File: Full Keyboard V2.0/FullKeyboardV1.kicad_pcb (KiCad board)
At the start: 2 copper layers, 305.6 x 104.9 mm, 624 parts, among them J1 Conn_01x26, J2 USB_C_Receptacle_USB2.0, P7 AMS1117, SW1 Esc, SW10 2, SW11 W, SW12 S, SW13 Z, SW15 3, SW16 E, SW17 D, SW18 X, SW19 4, SW2 Tab, SW20 R, SW21 F, SW22 C, SW23 5, SW24 T, SW25 G, SW26 V, SW27 6, SW28 Y, SW29 H, SW3 Caps, SW30 B, SW32 7, SW33 U, SW34 J, SW35 N, SW36 8, SW37 I, SW38 K, SW39 M, SW4 LShift, SW40 9, SW41 O, SW42 L, SW43 <, SW44 0, SW45 P, SW46 ;, SW47 >, SW49 Minus, SW5 End/Home, SW50 [, SW51 ", SW52 /, SW54 =, SW55 ], SW56 Up, SW57 RShift, SW59 BKSPC, SW6 1, SW60 \, SW61 Enter, SW63 Til, SW64 Del, SW65 Pg Up, SW66 Pg Dw, SW7 Q, SW8 A, T1 Vin, T3 Vout, U1 AT24C02, U3 CD74HC4067SM, U5 Cherry_bottom_row

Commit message: Added USB HUB
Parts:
- removed the REF**413 at (190.7, 60.1)
- removed the REF**413 at (180.7, 60.3)
- removed the REF**413 at (22.9, 59.1)
- removed the REF**413 at (41.6, 59.3)
- removed the REF**423 at (191.7, 60.1)
- removed the REF**423 at (42.6, 59.3)
- removed the REF**423 at (181.7, 60.3)
- removed the REF**423 at (23.9, 59.1)
- removed the REF**431 at (61.0, 58.9)
- removed the REF**431 at (80.7, 59.0)
- removed the REF**431 at (99.3, 58.9)
- removed the REF**431 at (118.3, 59.1)
- removed the REF**431 at (137.8, 59.0)
- removed the REF**431 at (157.2, 59.3)
- removed the REF**431 at (186.4, 56.0)
- removed the REF**432 at (129.7, 66.3)
- removed the REF**432 at (62.0, 58.9)
- removed the REF**432 at (81.7, 59.0)
- removed the REF**432 at (100.3, 58.9)
- removed the REF**432 at (119.3, 59.1)
- removed the REF**432 at (138.8, 59.0)
- removed the REF**432 at (158.2, 59.3)
- removed the REF**432 at (187.4, 56.0)
- removed the REF**433 at (159.2, 59.3)
- removed the REF**433 at (188.4, 56.0)
- removed the REF**433 at (129.7, 65.3)
- removed the REF**433 at (24.9, 59.1)
- removed the REF**433 at (43.6, 59.3)
- removed the REF**433 at (192.7, 60.1)
- removed the REF**433 at (182.7, 60.3)
- removed the REF**433 at (63.0, 58.9)
- removed the REF**433 at (82.7, 59.0)
- removed the REF**433 at (101.3, 58.9)
- removed the REF**433 at (120.3, 59.1)
- removed the REF**433 at (139.8, 59.0)
- added C3: 0.1uF, Capacitor_SMD:C_0603_1608Metric, B.Cu at (176.8, 55.6)
- added C74: 10uF, Capacitor_SMD:C_0603_1608Metric, B.Cu at (175.1, 55.6)
- added C75: 10uF, Capacitor_SMD:C_0603_1608Metric, B.Cu at (142.0, 52.0)
- added C76: 0.1uF, Capacitor_SMD:C_0603_1608Metric, B.Cu at (139.2, 52.0)
- added C77: 0.1uF, Capacitor_SMD:C_0603_1608Metric, B.Cu at (144.8, 52.0)
- added C78: 10uF, Capacitor_SMD:C_0603_1608Metric, B.Cu at (136.4, 52.0)
- added D69: Green, LED_SMD:LED_0603_1608Metric, F.Cu at (95.5, 53.0)
- added D73: Green, LED_SMD:LED_0603_1608Metric, F.Cu at (93.8, 53.0)
- added D74: Green, LED_SMD:LED_0603_1608Metric, F.Cu at (99.1, 53.0)
- added D75: Green, LED_SMD:LED_0603_1608Metric, F.Cu at (97.3, 53.0)
- added D76: Red, LED_SMD:LED_0603_1608Metric, F.Cu at (92.0, 53.0)
- added J3: USB_A, Connector_USB:USB_A_Stewart_SS-52100-001_Horizontal, B.Cu at (19.6, 55.1)
- added J4: USB_A, Connector_USB:USB_A_Stewart_SS-52100-001_Horizontal, B.Cu at (37.9, 55.1)
- added J5: USB_A, Connector_USB:USB_A_Stewart_SS-52100-001_Horizontal, B.Cu at (56.1, 55.1)
- added JP3: SolderJumper_2_Open, Jumper:SolderJumper-2_P1.3mm_Open_RoundedPad1.0x1.5mm, B.Cu at (187.8, 54.8)
- added JP4: SolderJumper_2_Open, Jumper:SolderJumper-2_P1.3mm_Open_RoundedPad1.0x1.5mm, B.Cu at (187.8, 51.0)
- added JP5: SolderJumper_2_Bridged, Jumper:SolderJumper-2_P1.3mm_Bridged_RoundedPad1.0x1.5mm, B.Cu at (180.6, 54.8)
- added JP6: SolderJumper_2_Bridged, Jumper:SolderJumper-2_P1.3mm_Bridged_RoundedPad1.0x1.5mm, B.Cu at (184.2, 51.0)
- added JP7: SolderJumper_2_Bridged, Jumper:SolderJumper-2_P1.3mm_Bridged_RoundedPad1.0x1.5mm, B.Cu at (180.6, 51.0)
- added JP8: SolderJumper_2_Bridged, Jumper:SolderJumper-2_P1.3mm_Bridged_RoundedPad1.0x1.5mm, B.Cu at (184.2, 54.8)
- added R10: 330, Resistor_SMD:R_0603_1608Metric, F.Cu at (106.2, 51.8)
- added R13: 330, Resistor_SMD:R_0603_1608Metric, F.Cu at (106.1, 54.8)
- added R14: 330, Resistor_SMD:R_0603_1608Metric, F.Cu at (89.1, 53.6)
- added R5: 100K, Resistor_SMD:R_0603_1608Metric, B.Cu at (176.0, 53.0)
- added R8: 47K, Resistor_SMD:R_0603_1608Metric, B.Cu at (175.8, 51.4)
- added R9: 2K7, Resistor_SMD:R_0603_1608Metric, B.Cu at (175.5, 49.7)
- added REF**431: Stitching-Via-0.6mm, keyboard:Stitching-Via-0.6mm, F.Cu at (239.7, 56.7)
- added REF**431: Stitching-Via-0.6mm, keyboard:Stitching-Via-0.6mm, F.Cu at (241.9, 56.7)
- added REF**431: Stitching-Via-0.6mm, keyboard:Stitching-Via-0.6mm, F.Cu at (248.0, 49.3)
- added REF**431: Stitching-Via-0.6mm, keyboard:Stitching-Via-0.6mm, F.Cu at (223.3, 71.7)
- added REF**432: Stitching-Via-0.6mm, keyboard:Stitching-Via-0.6mm, F.Cu at (223.3, 70.7)
- added REF**432: Stitching-Via-0.6mm, keyboard:Stitching-Via-0.6mm, F.Cu at (192.9, 49.2)
- added REF**432: Stitching-Via-0.6mm, keyboard:Stitching-Via-0.6mm, F.Cu at (192.2, 53.8)
- added REF**432: Stitching-Via-0.6mm, keyboard:Stitching-Via-0.6mm, F.Cu at (192.7, 60.7)
- added REF**433: Stitching-Via-0.6mm, keyboard:Stitching-Via-0.6mm, F.Cu at (223.3, 69.7)
- added REF**433: Stitching-Via-0.6mm, keyboard:Stitching-Via-0.6mm, F.Cu at (193.7, 60.7)
- added U2: FE1.1s, Package_SO:SSOP-28_3.9x9.9mm_P0.635mm, B.Cu at (168.3, 52.6)
- added Y1: 12MHz, Crystal:Crystal_SMD_HC49-SD, B.Cu at (153.6, 51.4)
- moved C2 2.46 mm to (196.3, 59.0)
- moved D40 1.93 mm to (167.0, 64.6), turned to 90 degrees
- moved D44 1.82 mm to (186.0, 64.5), turned to 90 degrees
- moved D36 1.62 mm to (148.1, 64.3), turned to 90 degrees
- moved D32 1.61 mm to (128.9, 64.2), turned to 90 degrees
- moved D10 1.05 mm to (34.2, 63.6), turned to 90 degrees
- moved D27 1.03 mm to (110.0, 63.7), turned to 90 degrees
- moved D15 1.01 mm to (53.1, 63.6), turned to 90 degrees
- moved D6 0.97 mm to (15.2, 63.6), turned to 90 degrees
- moved D23 0.97 mm to (91.0, 63.6), turned to 90 degrees
- moved D19 0.82 mm to (72.0, 63.5), turned to 90 degrees
- moved D1 0.27 mm to (-3.15, 63.0), turned to 90 degrees
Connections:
- J2 pad A6: /MicroSheet/USB+D+ -> /PowerSheet/USB_D+
- J2 pad A7: /MicroSheet/USB_D- -> /PowerSheet/USB_D-
- J2 pad B6: /MicroSheet/USB+D+ -> /PowerSheet/USB_D+
- J2 pad B7: /MicroSheet/USB_D- -> /PowerSheet/USB_D-
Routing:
- net +5V: track 47.9 -> 279.3 mm, vias 1 -> 4
- net Net-(J3-Pad2): track 0.00 -> 155.6 mm, vias 0 -> 2
- net Net-(J3-Pad3): track 0.00 -> 152.9 mm, vias 0 -> 2
- net Net-(J4-Pad2): track 0.00 -> 133.9 mm, vias 0 -> 2
- net Net-(J4-Pad3): track 0.00 -> 132.3 mm, vias 0 -> 2
- net Net-(J5-Pad2): track 0.00 -> 113.9 mm, vias 0 -> 1
- net Net-(J5-Pad3): track 0.00 -> 112.3 mm, vias 0 -> 1
- net /PowerSheet/USB_D+: track 0.00 -> 83.7 mm, vias 0 -> 4
- net Net-(D69-Pad1): track 0.00 -> 80.8 mm, vias 0 -> 1
- net /PowerSheet/USB_D-: track 0.00 -> 76.7 mm, vias 0 -> 4
- net Net-(R13-Pad2): track 0.00 -> 63.5 mm, vias 0 -> 1
- net Net-(R10-Pad2): track 0.00 -> 63.2 mm, vias 0 -> 1
- net Net-(C75-Pad2): track 0.00 -> 39.3 mm, vias 0 -> 4
- net +3V3: track 2497.4 -> 2528.2 mm, vias 74 -> 80
- net GND: track 19.3 -> 39.9 mm, vias 1 -> 2
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
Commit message: Added multi-function left and right shift
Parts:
- removed the REF**41 at (274.6, 130.3)
- removed the REF**41 at (248.4, 130.3)
- removed the REF**411 at (26.4, 122.0)
- removed the REF**411 at (254.2, 123.7)
- removed the REF**412 at (26.4, 123.0)
- removed the REF**412 at (254.2, 124.7)
- removed the REF**413 at (26.4, 124.0)
- removed the REF**413 at (5.54, 136.3)
- removed the REF**421 at (27.4, 122.0)
- removed the REF**421 at (255.2, 123.7)
- removed the REF**422 at (27.4, 123.0)
- removed the REF**422 at (255.2, 124.7)
- removed the REF**422 at (6.54, 135.3)
- removed the REF**423 at (27.4, 124.0)
- removed the REF**423 at (255.2, 125.7)
- removed the REF**431 at (28.4, 122.0)
- removed the REF**431 at (7.54, 134.3)
- removed the REF**432 at (28.4, 123.0)
- removed the REF**432 at (256.2, 124.7)
- removed the REF**433 at (28.4, 124.0)
- removed the REF**433 at (256.2, 125.7)
- removed SW56: Up, keyboard:RGB_CHERRY_PCB_100H
- removed SW57: RShift, keyboard:RGB_CHERRY_PCB_175H
- added C79: C_Small, Capacitor_SMD:C_0603_1608Metric, B.Cu at (21.1, 127.7)
- added D77: D_Small, Diode_SMD:D_SOD-123, B.Cu at (22.2, 116.0)
- added REF**41: Stitching-Via-0.6mm, keyboard:Stitching-Via-0.6mm, F.Cu at (32.1, 130.2)
- added SW9: double_key, keyboard:RGB_CHERRY_SHIFT_RIGHT_2.0, F.Cu at (252.4, 123.9)
- SW4: value LShift -> double_key; footprint keyboard:RGB_CHERRY_PCB_200H -> keyboard:RGB_CHERRY_SHIFT_ROW_LEFT
- moved C6 9.63 mm to (0.01, 129.0), turned to 90 degrees
- moved REF**41 8.97 mm to (11.2, 130.3)
- moved D4 5.96 mm to (9.66, 116.0)
- moved C61 4.11 mm to (241.3, 126.3)
- moved D57 3.07 mm to (237.0, 117.2)
- moved D56 1.22 mm to (261.0, 119.1)
- moved D9 1.13 mm to (21.1, 136.6)
- moved SW4 0.05 mm to (15.8, 123.9)
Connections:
- SW4 pad 3: +3V3 -> /ROW3
- SW4 pad 5: GND -> +3V3
- SW4 pad 6: Net-(SW13-Pad4) -> Net-(SW4-Pad6)
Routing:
- net Net-(SW56-Pad4): track 22.1 -> 0.00 mm, vias 2 -> 0
- net +3V3: track 2528.2 -> 2548.4 mm, vias 80 -> 81
- net Net-(SW13-Pad4): track 26.8 -> 10.5 mm
- net Net-(SW9-Pad10): track 0.00 -> 13.6 mm, vias 0 -> 2
- net Net-(SW4-Pad10): track 0.00 -> 13.0 mm, vias 0 -> 2
- net Net-(D4-Pad1): track 3.26 -> 15.1 mm
- net Net-(D57-Pad1): track 2.61 -> 13.9 mm
- net /ROW3: track 360.3 -> 369.9 mm
- net /COL0: track 291.6 -> 298.5 mm
- net Net-(D77-Pad1): track 0.00 -> 4.31 mm
- net Net-(SW66-Pad4): track 14.8 -> 10.8 mm
- net /COL1: track 276.1 -> 279.0 mm
- net /COL12: track 109.2 -> 106.7 mm
- net /COL13: track 136.0 -> 137.6 mm
- net Net-(D9-Pad1): track 6.98 -> 8.55 mm
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
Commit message: Added solder jumpers to allow for daisy chaining RGB rows
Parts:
- removed LCD2: SPI_spare, Connector_PinHeader_2.54mm:PinHeader_1x04_P2.54mm_Vertical_SMD_Pin1Left
- removed the REF**411 at (282.3, 53.2)
- removed the REF**421 at (282.3, 52.2)
- removed the REF**421 at (203.0, 97.4)
- removed the REF**431 at (239.7, 56.7)
- removed the REF**431 at (248.5, 53.3)
- removed the REF**431 at (203.0, 98.4)
- removed the REF**431 at (241.9, 56.7)
- removed the REF**431 at (248.0, 49.3)
- removed the REF**431 at (282.3, 51.2)
- removed the REF**432 at (192.7, 60.7)
- removed the REF**433 at (279.2, 117.5)
- removed the REF**433 at (279.2, 116.7)
- removed the REF**433 at (193.7, 60.7)
- added J6: Conn_01x04, Connector_JST:JST_PH_S4B-PH-SM4-TB_1x04-1MP_P2.00mm_Horizontal, B.Cu at (7.57, 53.7)
- added JP10: SolderJumper_2_Open, Jumper:SolderJumper-2_P1.3mm_Open_RoundedPad1.0x1.5mm, B.Cu at (9.69, 95.2)
- added JP11: SolderJumper_2_Open, Jumper:SolderJumper-2_P1.3mm_Open_RoundedPad1.0x1.5mm, B.Cu at (14.5, 114.0)
- added JP12: SolderJumper_2_Open, Jumper:SolderJumper-2_P1.3mm_Open_RoundedPad1.0x1.5mm, B.Cu at (8.72, 133.3)
- added JP9: SolderJumper_2_Open, Jumper:SolderJumper-2_P1.3mm_Open_RoundedPad1.0x1.5mm, B.Cu at (0.99, 76.0)
- added REF**413: Stitching-Via-0.6mm, keyboard:Stitching-Via-0.6mm, F.Cu at (76.9, 53.7)
- added REF**423: Stitching-Via-0.6mm, keyboard:Stitching-Via-0.6mm, F.Cu at (75.9, 53.7)
- added REF**431: Stitching-Via-0.6mm, keyboard:Stitching-Via-0.6mm, F.Cu at (283.3, 61.1)
- added REF**431: Stitching-Via-0.6mm, keyboard:Stitching-Via-0.6mm, F.Cu at (286.8, 53.1)
- added REF**431: Stitching-Via-0.6mm, keyboard:Stitching-Via-0.6mm, F.Cu at (281.9, 53.0)
- added REF**432: Stitching-Via-0.6mm, keyboard:Stitching-Via-0.6mm, F.Cu at (284.3, 61.1)
- added REF**432: Stitching-Via-0.6mm, keyboard:Stitching-Via-0.6mm, F.Cu at (198.8, 50.7)
- added REF**432: Stitching-Via-0.6mm, keyboard:Stitching-Via-0.6mm, F.Cu at (286.8, 54.1)
- added REF**432: Stitching-Via-0.6mm, keyboard:Stitching-Via-0.6mm, F.Cu at (281.9, 54.0)
- added REF**433: Stitching-Via-0.6mm, keyboard:Stitching-Via-0.6mm, F.Cu at (285.3, 61.1)
- added REF**433: Stitching-Via-0.6mm, keyboard:Stitching-Via-0.6mm, F.Cu at (74.9, 53.7)
- added REF**433: Stitching-Via-0.6mm, keyboard:Stitching-Via-0.6mm, F.Cu at (286.8, 55.1)
- added REF**433: Stitching-Via-0.6mm, keyboard:Stitching-Via-0.6mm, F.Cu at (281.9, 55.0)
- J1: value Conn_01x26 -> Conn_01x30; footprint Connector_FFC-FPC:Hirose_FH12-26S-0.5SH_1x26-1MP_P0.50mm_Horizontal -> Connector_FFC-FPC:Hirose_FH12-30S-0.5SH_1x30-1MP_P0.50mm_Horizontal
- moved REF**41 17.2 mm to (15.0, 130.3)
- moved C79 15.2 mm to (34.7, 121.0), turned to 180 degrees
- moved REF**41 14.8 mm to (26.0, 130.0)
- moved D63 6.67 mm to (279.3, 63.6), turned to 135 degrees
- moved D9 1.86 mm to (22.9, 136.5)
- moved J1 1.01 mm to (217.7, 51.4)
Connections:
- net Net-(U5-Pad4) renamed /RGB4_OUT
- SW1 pad 4: Net-(SW1-Pad4) -> /RGB0_OUT
- SW2 pad 4: Net-(SW2-Pad4) -> /RGB1_OUT
- SW3 pad 4: Net-(SW3-Pad4) -> /RGB2_OUT
- SW4 pad 6: Net-(SW4-Pad6) -> /RGB3_OUT
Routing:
- net /MicroSheet/MOUSE_X: track 0.00 -> 371.8 mm, vias 0 -> 2
- net /RGB1: track 117.4 -> 412.9 mm, vias 2 -> 3
- net /RGB4: track 173.9 -> 468.9 mm, vias 2 -> 3
- net /RGB2: track 136.8 -> 425.2 mm, vias 2 -> 3
- net /RGB3: track 155.2 -> 440.8 mm, vias 2 -> 3
- net /MicroSheet/MOUSE_Y: track 0.00 -> 269.9 mm, vias 0 -> 2
- net GND: track 39.9 -> 67.7 mm, vias 4 -> 11
- net /COL14: track 219.8 -> 242.5 mm
- net SDA: track 71.6 -> 61.2 mm
- net Net-(SW4-Pad10): track 13.0 -> 4.19 mm
- net /RGB2_OUT: track 0.00 -> 7.72 mm
- net /MicroSheet/MUX1: track 9.80 -> 16.5 mm
- net /MicroSheet/MUX0: track 11.4 -> 18.0 mm
- net /ROW0: track 312.4 -> 318.8 mm
- net Net-(SW13-Pad4): track 10.5 -> 15.9 mm
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
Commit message: Updated footprints on keyboard PCB
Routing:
- net /ROW3: track 368.0 -> 377.5 mm
- net /COL12: track 106.7 -> 107.8 mm

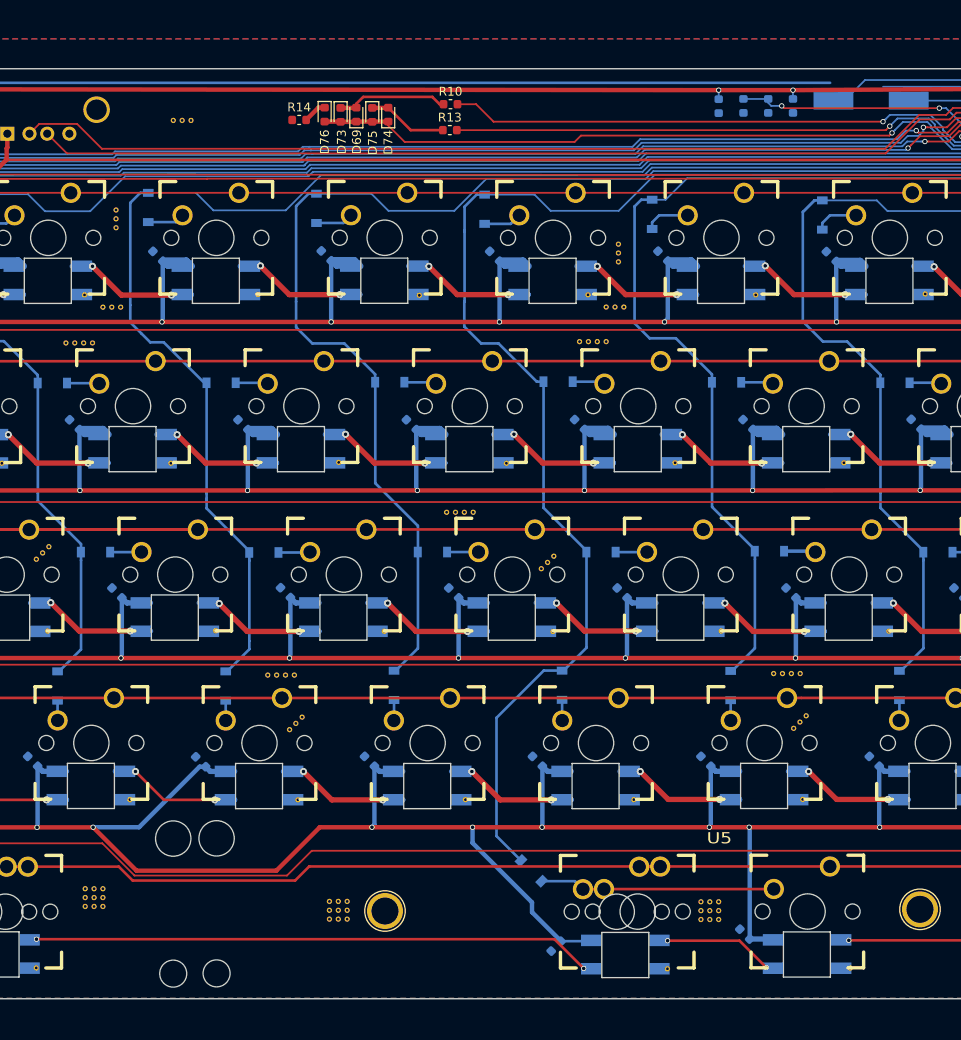
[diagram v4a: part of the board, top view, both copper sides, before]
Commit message: Updated bluepill board for 30pin ribbon cable
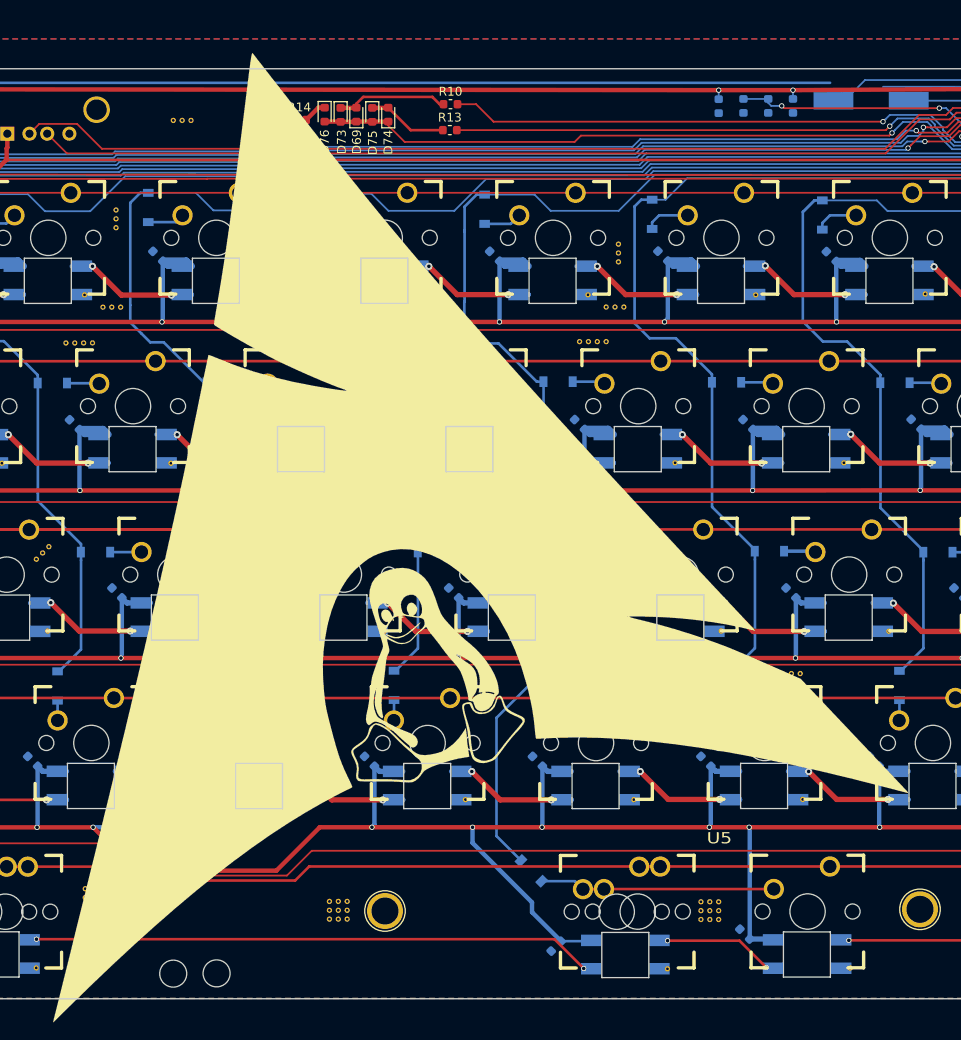
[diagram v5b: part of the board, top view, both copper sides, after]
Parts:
- added G***: LOGO, keyboard:tux, B.Cu at (102.9, 115.8)
- added G***: LOGO, keyboard:arch, B.Cu at (97.1, 94.7)
- added G***: LOGO, keyboard:tux, F.Cu at (102.6, 115.8)
- added G***: LOGO, keyboard:arch, F.Cu at (97.1, 94.6)
